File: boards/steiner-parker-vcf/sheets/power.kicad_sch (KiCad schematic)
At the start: 7 parts, among them J1 Eurorack Power, J3 Conn_02x08_Odd_Even

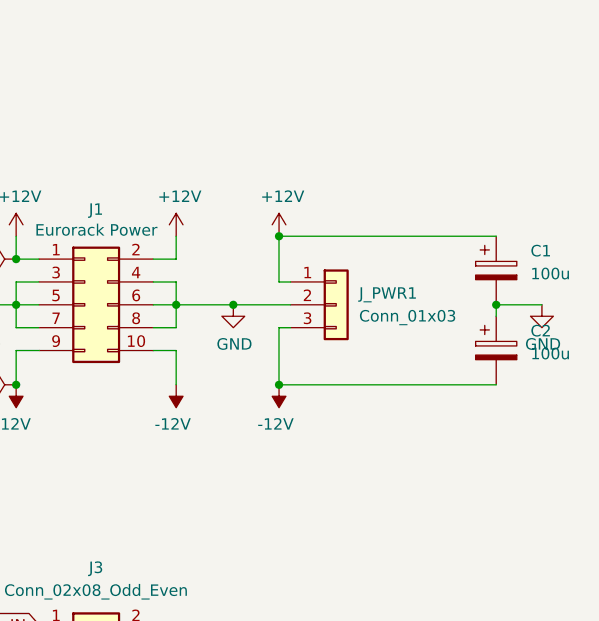
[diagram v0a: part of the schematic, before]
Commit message: Added production files for VCF
ref https://github.com/shmoergh/hog/issues/19
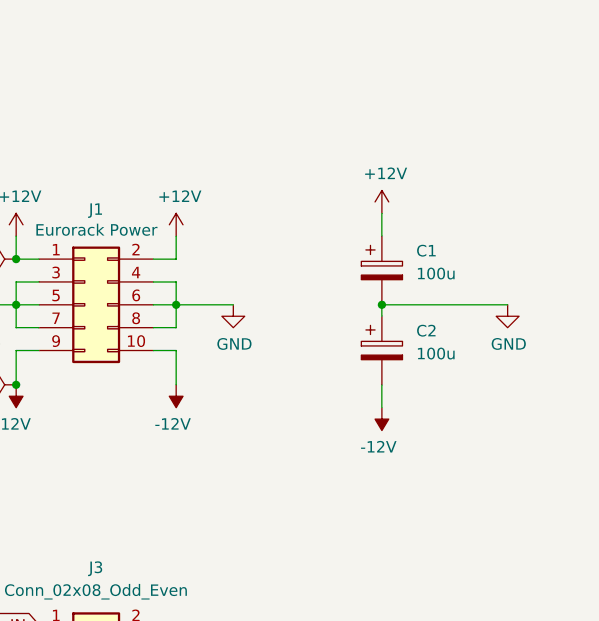
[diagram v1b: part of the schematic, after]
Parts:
- removed J_PWR1: Conn_01x03, Connector_PinHeader_2.54mm:PinHeader_1x03_P2.54mm_Vertical, symbol Connector_Generic:Conn_01x03
- C1, C2: footprint Capacitor_THT:CP_Radial_D6.3mm_P2.50mm -> Capacitor_SMD:CP_Elec_6.3x7.7; FT Rotation Offset (none) -> 180; LCSC (none) -> C2836437; Vendor (none) -> JLCPCB; now in the parts list
- J1: Part No. (none) -> 737-RS2-10-G; Part URL (none) -> https://mou.sr/3ZTZokP; Vendor (none) -> Mouser; now in the parts list
- J3: Part No. (none) -> 737-RS2-16-G; Part URL (none) -> https://mou.sr/3DcrsXN; Vendor (none) -> Mouser; now in the parts list
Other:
- moved on the sheet: C1
